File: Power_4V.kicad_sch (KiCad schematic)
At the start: 9 parts, among them U2 AP63200WU

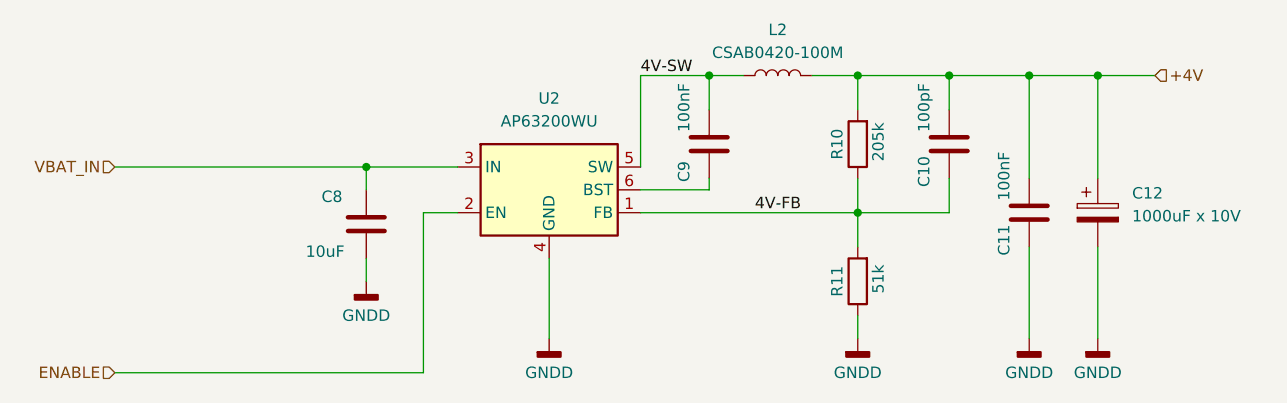
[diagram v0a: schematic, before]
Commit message: Replace SIM800DC with A7682E
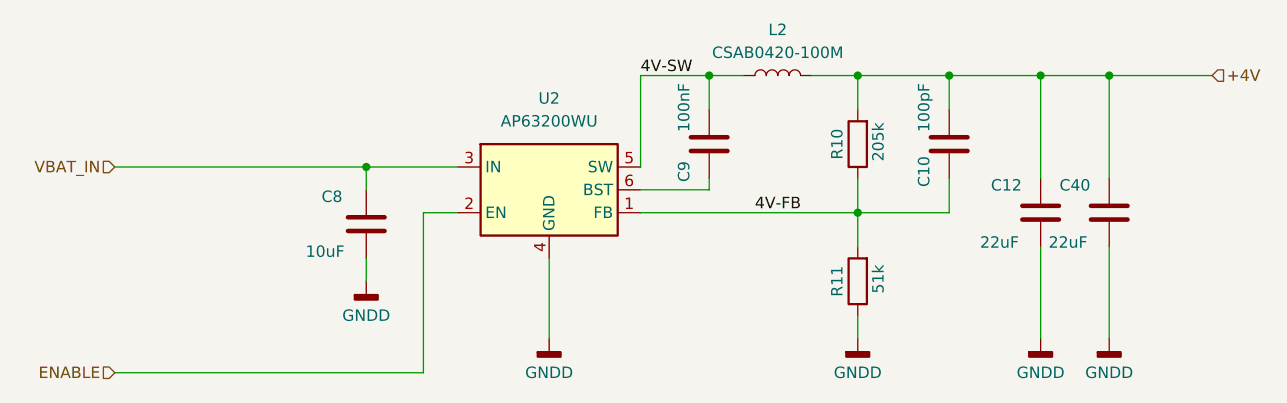
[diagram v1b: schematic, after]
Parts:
- removed C11: 100nF, Capacitor_SMD:C_0805_2012Metric_Pad1.18x1.45mm_HandSolder, symbol Device:C
- removed C12: 1000uF x 10V, Capacitor_SMD:CP_Elec_10x10.5, symbol Device:C_Polarized
- added C12, C40: 22uF, Capacitor_SMD:C_0805_2012Metric_Pad1.18x1.45mm_HandSolder, symbol Device:C
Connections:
- net +4V: now also C12.2, C40.2
- net GNDD: now also C12.1, C40.1
